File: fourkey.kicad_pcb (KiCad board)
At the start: 2 copper layers, 85.3 x 75.7 mm, 23 parts, among them K1 KEYSW, K2 KEYSW, K3 KEYSW, K4 KEYSW, SW1 SW_PUSH, U1 ProMicro

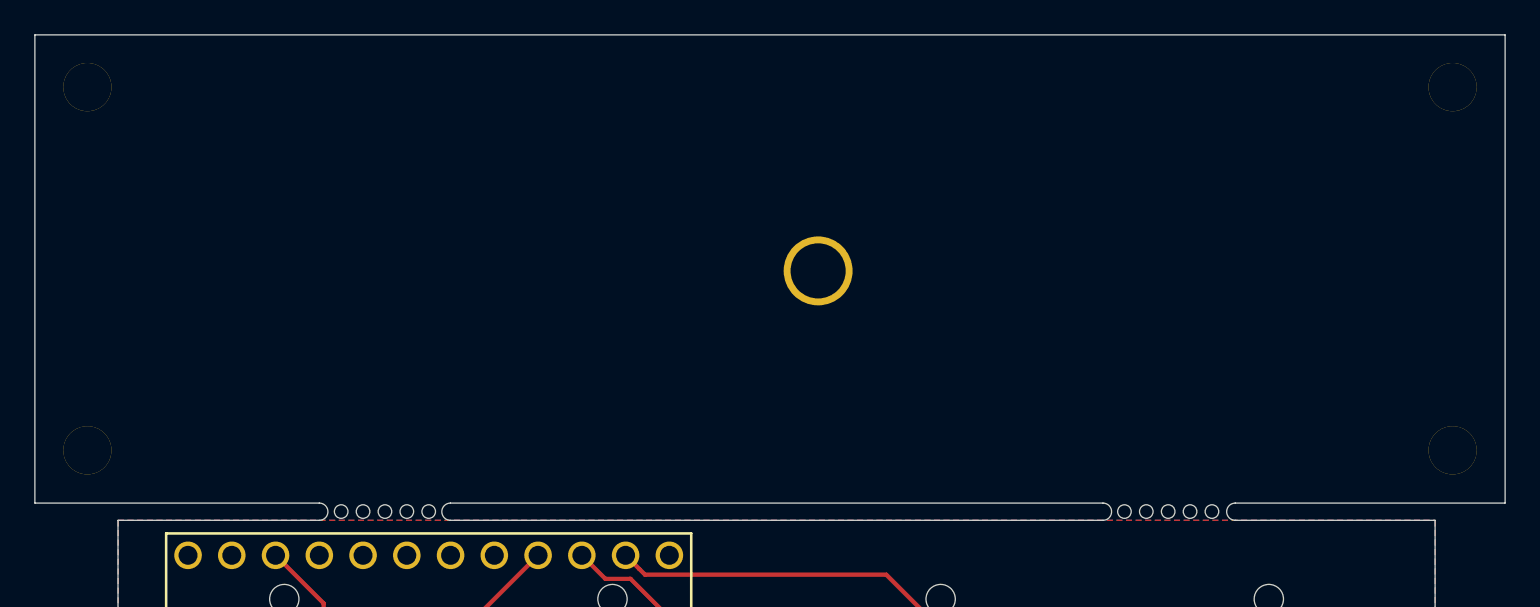
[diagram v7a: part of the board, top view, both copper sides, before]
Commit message: more rounded corners
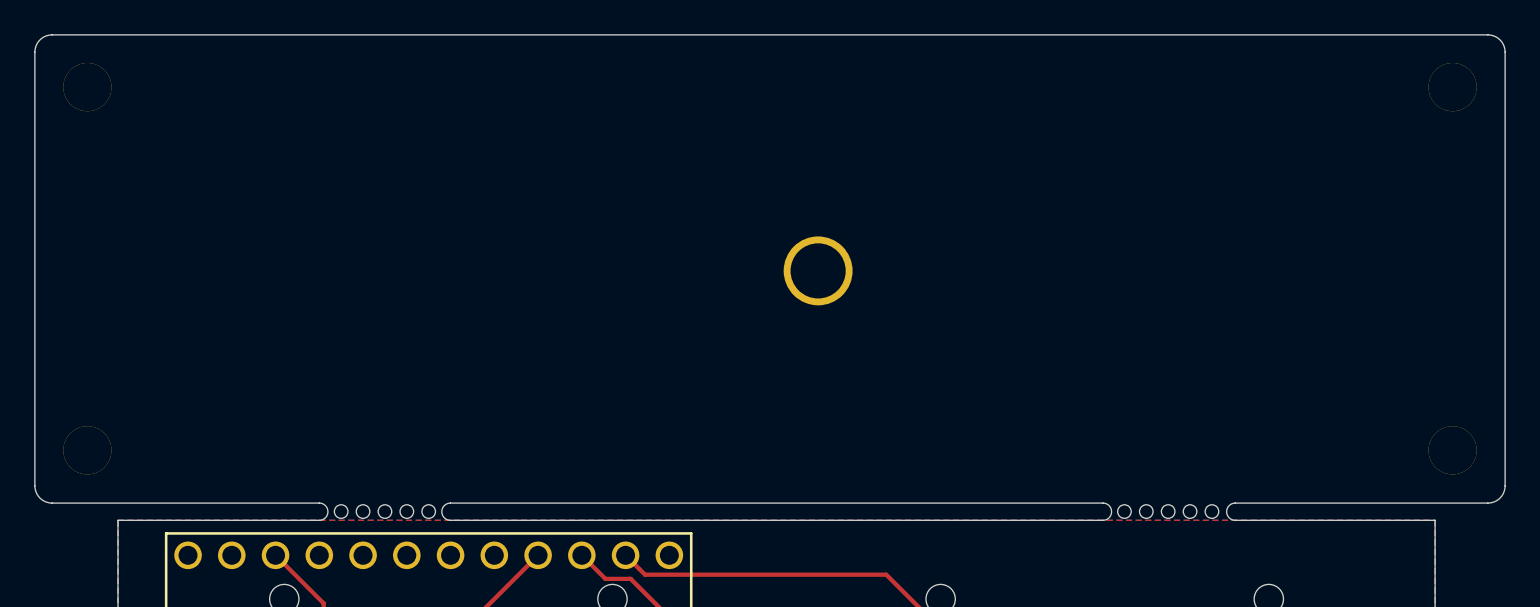
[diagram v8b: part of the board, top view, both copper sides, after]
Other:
- outline, holes or cut-outs redrawn
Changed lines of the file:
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@@
   (general
     (thickness 1.6)
-    (drawings 32)
+    (drawings 36)
     (tracks 38)
     (zones 0)
@@
     )
   )
+  (gr_arc (start 211.344 74.708) (end 212.344 74.708) (angle 90) (layer Edge.Cuts) (width 0.05))
+  (gr_arc (start 211.344 49.53) (end 211.344 48.53) (angle 90) (layer Edge.Cuts) (width 0.05))
+  (gr_arc (start 128 49.53) (end 128 48.53) (angle -90) (layer Edge.Cuts) (width 0.05))
+  (gr_arc (start 128 74.708) (end 127 74.708) (angle -90) (layer Edge.Cuts) (width 0.05))
   (gr_arc (start 211.344 98.012) (end 212.344 98.012) (angle -90) (layer Edge.Cuts) (width 0.05))
   (gr_arc (start 211.344 123.19) (end 212.344 123.19) (angle 90) (layer Edge.Cuts) (width 0.05))
@@
   (gr_line (start 151.122 96.012) (end 189 96.012) (layer Edge.Cuts) (width 0.05))
   (gr_line (start 189 76.708) (end 151.122 76.708) (layer Edge.Cuts) (width 0.05))
-  (gr_line (start 196.68 75.708) (end 212.344 75.708) (layer Edge.Cuts) (width 0.05))
+  (gr_line (start 196.68 75.708) (end 211.344 75.708) (layer Edge.Cuts) (width 0.05))
   (gr_line (start 143.51 76.708) (end 131.826 76.708) (layer Edge.Cuts) (width 0.05))
   (gr_line (start 151.122 75.708) (end 189 75.708) (layer Edge.Cuts) (width 0.05))
-  (gr_line (start 212.344 48.53) (end 127 48.53) (layer Edge.Cuts) (width 0.05))
-  (gr_line (start 127 48.53) (end 127 75.708) (layer Edge.Cuts) (width 0.05))
-  (gr_line (start 127 75.708) (end 143.51 75.708) (layer Edge.Cuts) (width 0.05))
-  (gr_line (start 212.344 75.708) (end 212.344 48.53) (layer Edge.Cuts) (width 0.05))
+  (gr_line (start 211.344 48.53) (end 128 48.53) (layer Edge.Cuts) (width 0.05))
+  (gr_line (start 127 49.53) (end 127 74.708) (layer Edge.Cuts) (width 0.05))
+  (gr_line (start 128 75.708) (end 143.51 75.708) (layer Edge.Cuts) (width 0.05))
+  (gr_line (start 212.344 74.708) (end 212.344 49.53) (layer Edge.Cuts) (width 0.05))
   (gr_line (start 208.28 96.012) (end 208.28 76.708) (layer Edge.Cuts) (width 0.05))
   (gr_line (start 131.826 96.012) (end 143.51 96.012) (layer Edge.Cuts) (width 0.05))
